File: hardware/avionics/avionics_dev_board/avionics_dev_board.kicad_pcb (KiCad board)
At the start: 4 copper layers, 113.6 x 79.4 mm, 78 parts, among them IC1 ADXL375BCCZ, IC2 W25Q256JVEIQ, J1 Main battery, J10 Parachute battery, J2 LAMBDA62, J3 Conn_01x08_Socket, J4 LAMBDA80, J5 Conn_01x08_Socket, J6 SWD interface, J7 868MHz antenna, J8 2.4GHz antenna, J9 Nichrome connector, Q3 FDS2734, SW2 SW_SPDT, SW3 SW_SPDT, SW4 SW_Push, SW5 SW_SPDT, U1 TPS563200, U2 MMC5983MA, U3 LSM6DSR, U4 BMP581, U6 MAX-M10S-00B, U7 STM32G474RET6, Y1 16MHz

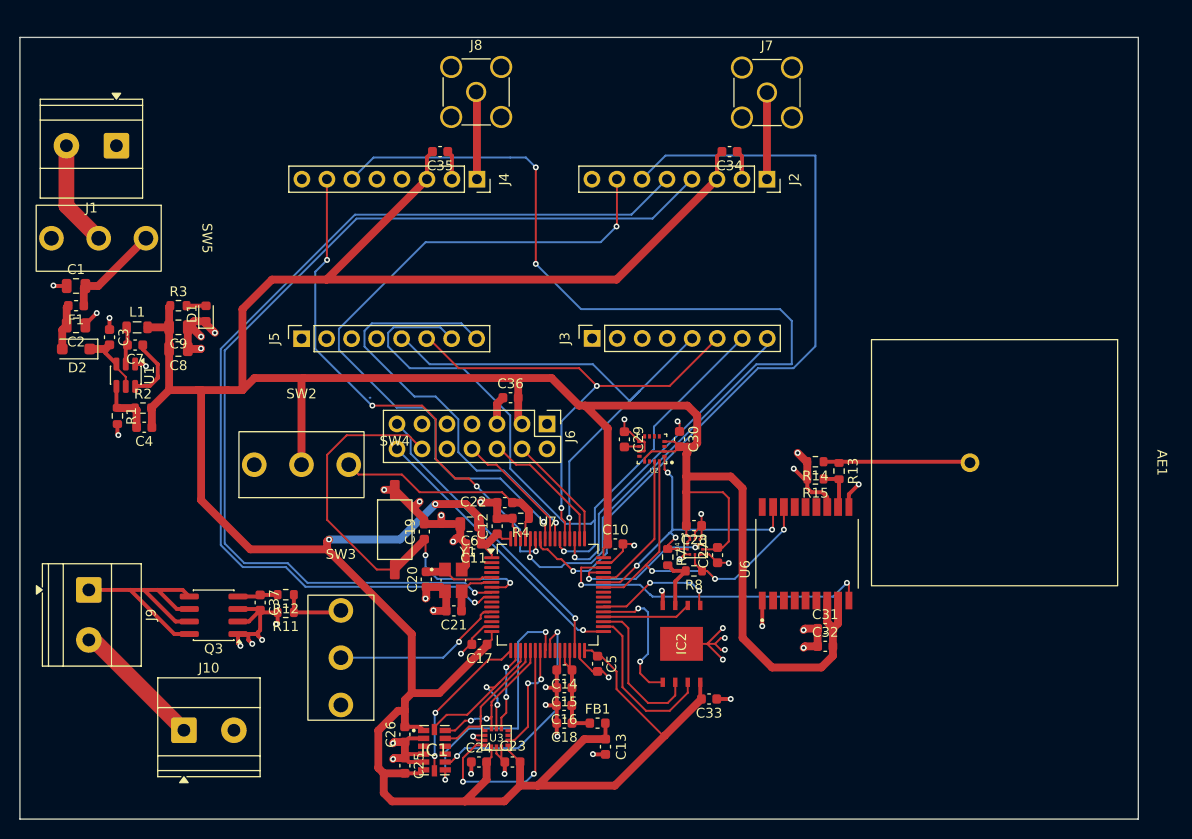
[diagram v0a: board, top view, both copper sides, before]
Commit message: Avionics dev PCB revision 2 - improved stackup and routing
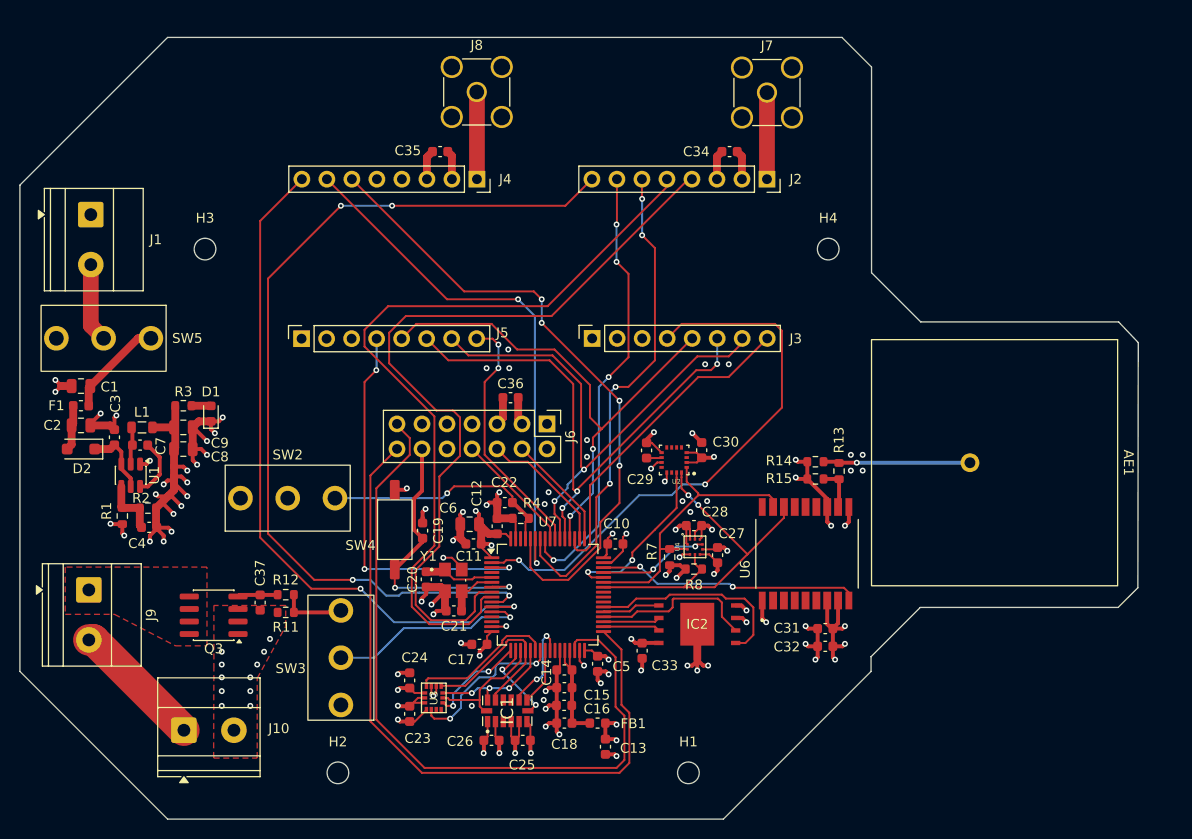
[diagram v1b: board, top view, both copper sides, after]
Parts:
- added H1: MountingHole, MountingHole:MountingHole_2.2mm_M2, F.Cu at (166.5, 102.5)
- added H2: MountingHole, MountingHole:MountingHole_2.2mm_M2, F.Cu at (130.9, 102.5)
- added H3: MountingHole, MountingHole:MountingHole_2.2mm_M2, F.Cu at (117.4, 49.3)
- added H4: MountingHole, MountingHole:MountingHole_2.2mm_M2, F.Cu at (180.7, 49.3)
- moved C25 12.2 mm to (149.7, 99.2), turned to 0 degrees
- moved C23 11.5 mm to (138.2, 96.5), turned to -90 degrees
- moved C24 10.9 mm to (138.2, 93.1), turned to -90 degrees
- moved C2 10.2 mm to (104.8, 67.2)
- moved C7 10.2 mm to (110.8, 69.2)
- moved F1 10.2 mm to (104.8, 65.2)
- moved R3 10.2 mm to (115.2, 65.2)
- moved U1 10.2 mm to (109.8, 72.3)
- moved C1 10.2 mm to (104.8, 63.2)
- moved D1 10.2 mm to (118.0, 66.0)
- moved C3 10.2 mm to (108.2, 68.4)
- moved C4 10.2 mm to (111.7, 77.6)
- moved C8 10.2 mm to (115.2, 69.6)
- moved C9 10.2 mm to (115.2, 67.4)
- moved D2 10.2 mm to (104.8, 69.6)
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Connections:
- net Net-(J10-Pin_1) renamed /PARA_PWR
- net Net-(J9-Pin_1) renamed /PARA_GND
- J3 pad 1: /L62_DIO3 -> unconnected-(J3-Pin_1-Pad1)
- J5 pad 1: /L80_DIO3 -> unconnected-(J5-Pin_1-Pad1)
- U7 pad 10: /L62_DIO3 -> /L62_DIO2
- U7 pad 11: /L80_DIO3 -> /L80_DIO2
- U7 pad 17: /CS_ADXL -> /CS_LSM6
- U7 pad 18: /CS_LSM6 -> /CS_ADXL
- U7 pad 4: /L62_DIO2 -> unconnected-(U7-PC15-Pad4)
- U7 pad 62: /L80_DIO2 -> unconnected-(U7-PB9-Pad62)
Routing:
- net +3V3: track 439.4 -> 110.8 mm, vias 2 -> 32
- net /L62_DIO2: track 0.00 -> 92.4 mm, vias 0 -> 4
- net /L80_DIO2: track 0.15 -> 70.5 mm, vias 0 -> 2
- net /L62_RST: track 0.00 -> 57.2 mm, vias 0 -> 2
- net /VCP_RX: track 30.7 -> 76.2 mm, vias 1 -> 0
- net /VCP_TX: track 28.7 -> 72.1 mm, vias 1 -> 0
- net /L80_RST: track 0.00 -> 40.4 mm, vias 0 -> 3
- net /L80_BUSY: track 102.1 -> 65.6 mm, vias 3 -> 4
- net /L62_BUSY: track 79.2 -> 50.5 mm, vias 1 -> 4
- net /PARA_GND: track 28.3 -> 0.00 mm
- net /L62_DIO1: track 71.6 -> 45.5 mm, vias 2 -> 4
- net /L62_RXSW: track 103.5 -> 81.1 mm, vias 1 -> 0
- net /L62_TXSW: track 102.6 -> 80.3 mm, vias 1 -> 0
- net /INT1_ADXL: track 26.1 -> 5.79 mm, vias 2 -> 0
- net /L80_CS: track 44.4 -> 25.7 mm, vias 1 -> 2
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- added copper zone on In2.Cu, net +3V3
- added copper zone on F.Cu, net /PARA_GND
- added copper zone on F.Cu, net GND
- removed copper zone on In2.Cu, net GND
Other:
- outline, holes or cut-outs redrawn

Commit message: Cleanup and refinements to avionics dev board PCB
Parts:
- moved C4 104.8 mm to (207.9, 36.2), turned to -90 degrees
- moved R1 104.8 mm to (206.8, 38.9), turned to 0 degrees
- moved R2 102.3 mm to (206.0, 36.3), turned to 90 degrees
- moved J1-MBAT 99.6 mm to (205.1, 53.9), turned to 90 degrees
- moved BUCK 98.9 mm to (202.7, 38.0), turned to 0 degrees
- moved D2 98.8 mm to (200.0, 43.1), turned to -90 degrees
- moved C2 95.9 mm to (197.6, 43.1), turned to -90 degrees
- moved C3 95.0 mm to (198.8, 39.7), turned to 0 degrees
- moved C7 94.4 mm to (199.6, 37.1), turned to -90 degrees
- moved F1 93.5 mm to (195.6, 43.1), turned to -90 degrees
- moved C8 92.5 mm to (200.0, 32.7), turned to -90 degrees
- moved L1 92.0 mm to (197.8, 36.9), turned to 90 degrees
- moved C1 91.1 mm to (193.6, 43.1), turned to 90 degrees
- moved C9 89.6 mm to (197.8, 32.7), turned to -90 degrees
- moved R3 86.7 mm to (195.6, 32.7), turned to 90 degrees
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- renumbered IC1 to ADXL, J8 to ANT_24, J7 to ANT_868, U4 to BMP1, SW2 to BOOT_SW, U1 to BUCK, J1 to J1-MBAT, J10 to J10-PBAT, J9 to J9-NICH, J2 to L62-1, J3 to L62-2, J4 to L80-1, J5 to L80-2, U3 to LSM6, U6 to M10S, U7 to MCU, U2 to MMC, SW3 to PARA_ARM, D1 to PWR_LED, SW5 to PWR_SW, SW4 to RST, J6 to SWD_INT, IC2 to W25Q
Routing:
- net Net-(PARA_ARM1-C): track 6.66 -> 55.0 mm, vias 0 -> 1
- net Net-(J1-MBAT1-Pin_2): track 8.02 -> 27.8 mm
- net /PARA_PWR: track 13.5 -> 6.96 mm
- net /SPI1_SCK: track 12.8 -> 13.7 mm, vias 0 -> 1
- net /I2C2_SCL: track 30.4 -> 30.5 mm, vias 0 -> 1
- net /LSM6_INT1: vias 0 -> 1
- net /L62_CS: vias 0 -> 1
- net GND: vias 86 -> 189
- net /SPI2_SCK: vias 0 -> 1
- net /SPI2_MOSI: vias 0 -> 1
- net /SPI2_MISO: vias 0 -> 1
- net /SPI1_MISO: vias 0 -> 1
- net /RST_W25Q: vias 0 -> 1
- net /L62_TXSW: vias 0 -> 1
- net /L62_RXSW: vias 0 -> 1
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- added copper zone on B.Cu, net GND
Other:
- board size 113.6 x 79.4 mm -> 91.5 x 78.9 mm

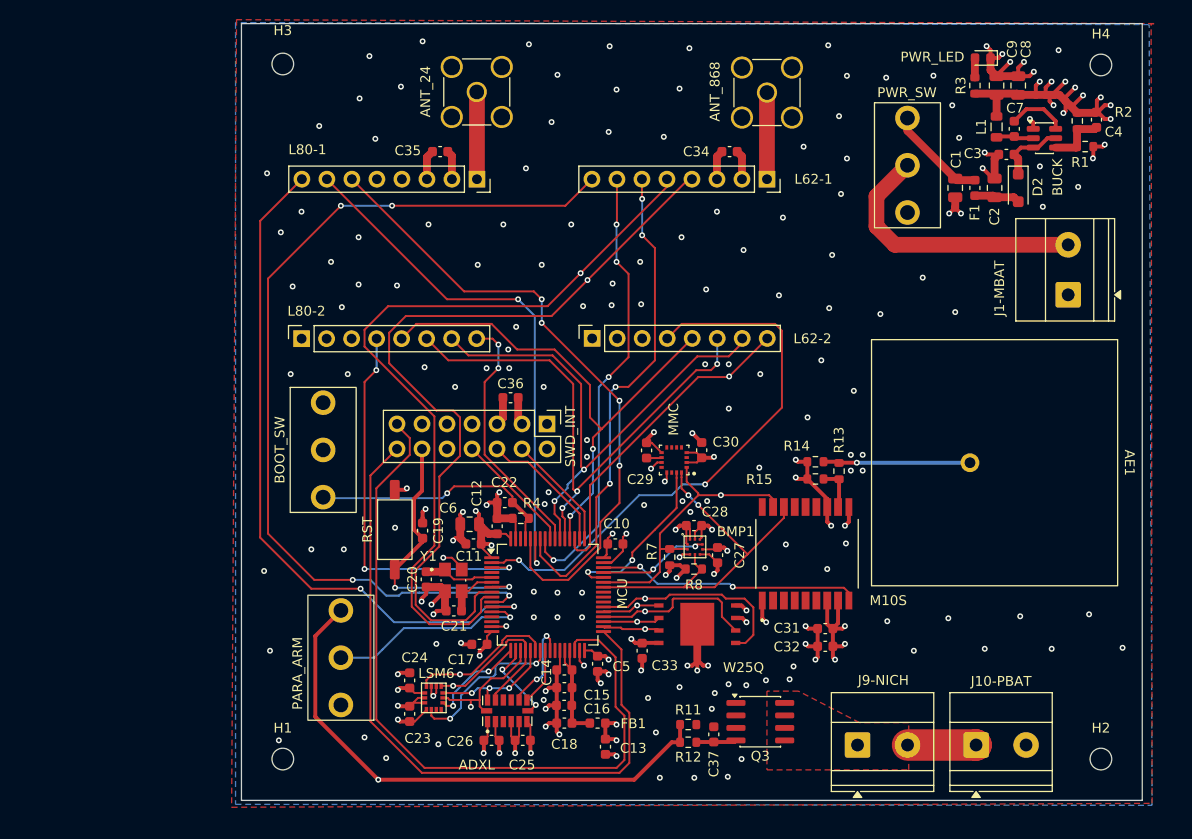
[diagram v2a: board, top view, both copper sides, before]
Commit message: Improved shielding of GPS RF trace and added 0 ohm resistors to switch SWD RX and TX if necessary
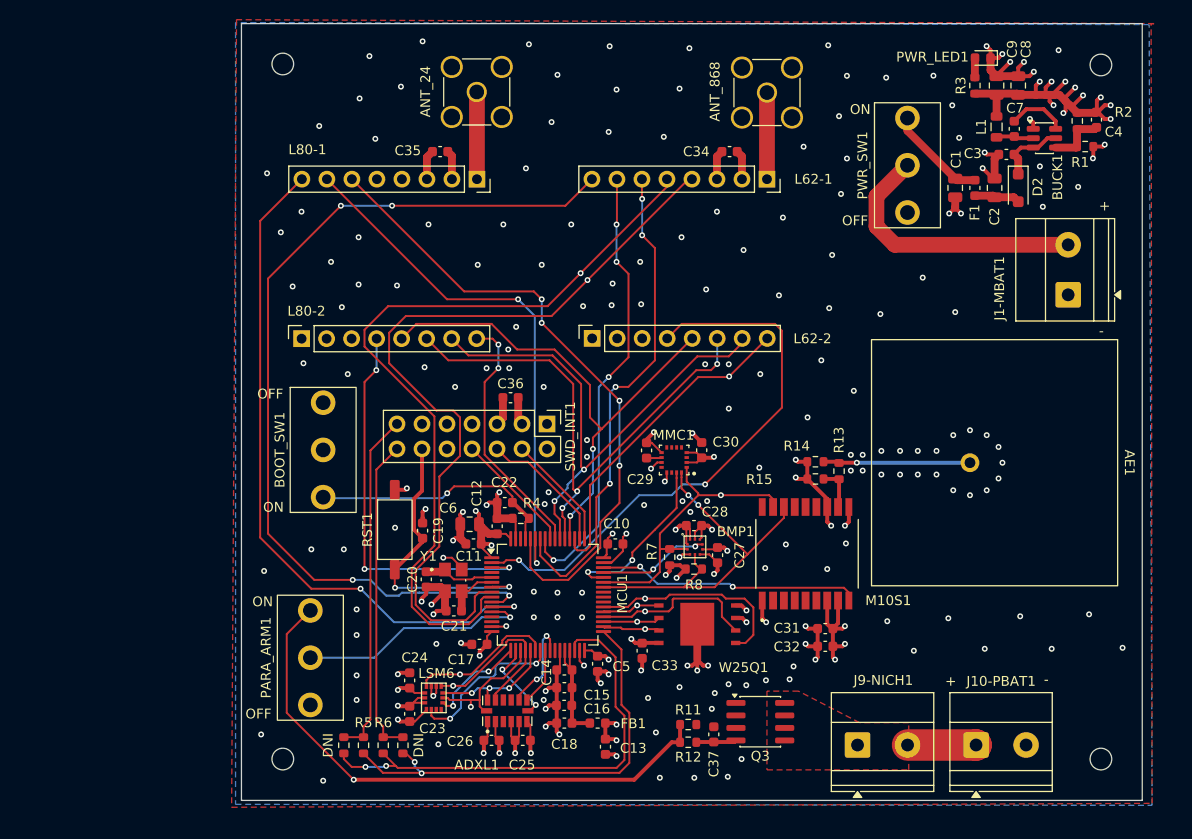
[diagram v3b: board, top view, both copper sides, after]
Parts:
- added DNI: 0R, Resistor_SMD:R_0603_1608Metric, F.Cu at (131.5, 99.7)
- added DNI: 0R, Resistor_SMD:R_0603_1608Metric, F.Cu at (137.5, 99.7)
- added R5: 0R, Resistor_SMD:R_0603_1608Metric, F.Cu at (133.5, 99.7)
- added R6: 0R, Resistor_SMD:R_0603_1608Metric, F.Cu at (135.5, 99.7)
- C20, C21: value 10pF -> 12pF
- moved PARA_ARM1 3.10 mm to (128.1, 90.8)
- renumbered ADXL to ADXL1, BOOT_SW to BOOT_SW1, BUCK to BUCK1, J1-MBAT to J1-MBAT1, J10-PBAT to J10-PBAT1, J9-NICH to J9-NICH1, M10S to M10S1, MCU to MCU1, MMC to MMC1, PARA_ARM to PARA_ARM1, PWR_LED to PWR_LED1, PWR_SW to PWR_SW1, RST to RST1, SWD_INT to SWD_INT1, W25Q to W25Q1
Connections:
- MCU1 pad 30: /VCP_RX -> /VCP_TX
- MCU1 pad 33: /VCP_TX -> /VCP_RX
- SWD_INT1 pad 13: /VCP_RX -> Net-(SWD_INT1-Pin_13)
- SWD_INT1 pad 14: /VCP_TX -> Net-(SWD_INT1-Pin_14)
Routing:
- net Net-(SWD_INT1-Pin_13): track 0.00 -> 35.4 mm
- net Net-(SWD_INT1-Pin_14): track 0.00 -> 32.4 mm
- net /VCP_RX: track 76.2 -> 45.7 mm, vias 0 -> 2
- net /VCP_TX: track 72.1 -> 48.3 mm, vias 0 -> 2
- net /PARA_DEPLOY: track 21.0 -> 24.1 mm
- net Net-(PARA_ARM1-C): track 55.0 -> 57.5 mm
- net GND: vias 189 -> 208
- added copper zone on In2.Cu, net GND
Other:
- board text added: "+"
- board text added: "-"
- board text added: "OFF"
- board text added: "ON"

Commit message: Added pull up/down resistors to some pins according to datasheet recommendations
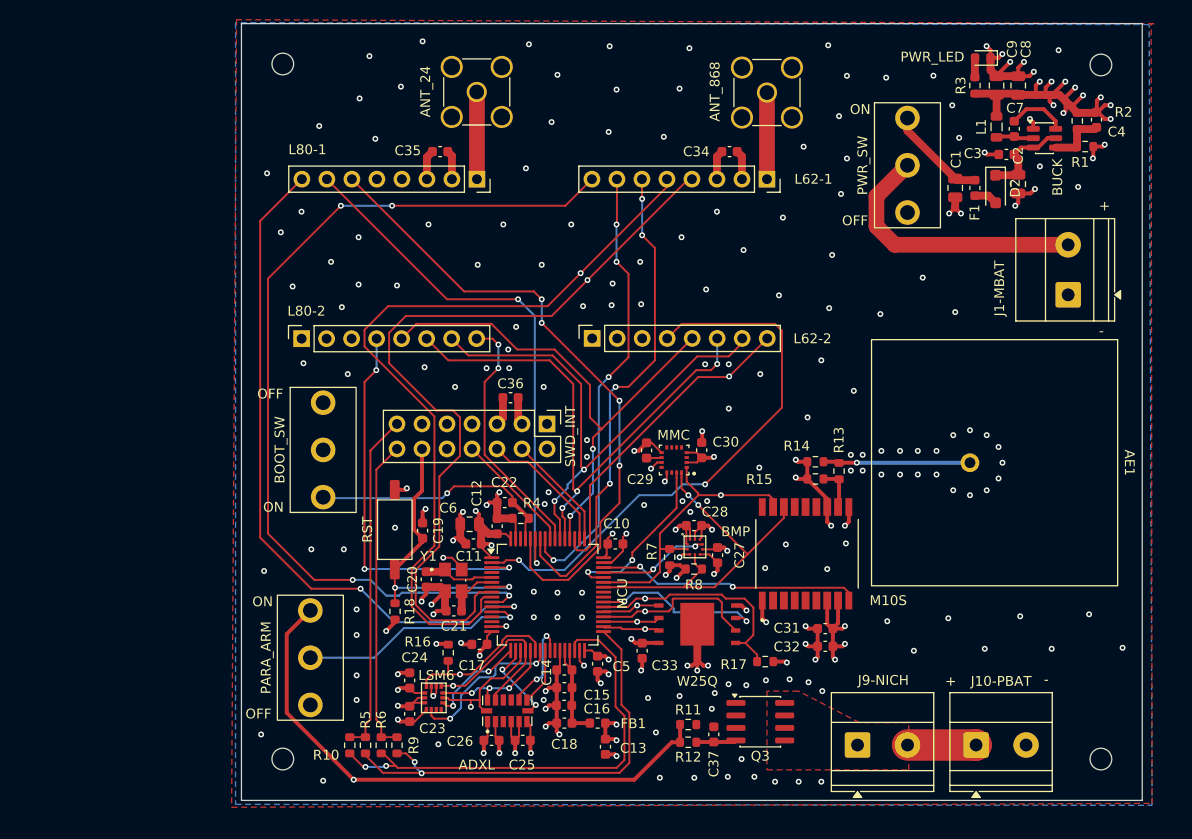
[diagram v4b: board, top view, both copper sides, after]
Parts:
- added R16: 10kR, Resistor_SMD:R_0603_1608Metric, F.Cu at (142.1, 90.3)
- added R17: 10kR, Resistor_SMD:R_0603_1608Metric, F.Cu at (174.3, 91.2)
- added R18: 10kR, Resistor_SMD:R_0603_1608Metric, F.Cu at (136.7, 86.1)
- moved C2 2.43 mm to (200.0, 42.7), turned to 90 degrees
- moved D2 2.30 mm to (197.7, 43.2)
- moved R10 0.60 mm to (132.1, 99.7)
- moved R9 0.60 mm to (136.9, 99.7)
- moved R5 0.20 mm to (133.7, 99.7)
- moved R6 0.20 mm to (135.3, 99.7)
- renumbered ADXL1 to ADXL, BMP1 to BMP, BOOT_SW1 to BOOT_SW, BUCK1 to BUCK, J1-MBAT1 to J1-MBAT, J10-PBAT1 to J10-PBAT, J9-NICH1 to J9-NICH, M10S1 to M10S, MCU1 to MCU, MMC1 to MMC, PARA_ARM1 to PARA_ARM, PWR_LED1 to PWR_LED, PWR_SW1 to PWR_SW, DNI to R10, DNI to R9, RST1 to RST, SWD_INT1 to SWD_INT, W25Q1 to W25Q
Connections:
- net /RST_W25Q renamed /HOLD_W25Q
- C2 pad 2: Net-(D2-A) -> Net-(BUCK1-EN)
- MCU pad 39: unconnected-(MCU1-PC7-Pad39) -> /WP_W25Q
- W25Q pad 3: +3V3 -> /WP_W25Q
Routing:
- net /WP_W25Q: track 0.00 -> 17.6 mm, vias 0 -> 2
- net Net-(BUCK1-EN): track 7.08 -> 9.63 mm
- net /CS_W25Q: track 21.2 -> 23.6 mm
- net Net-(D2-A): track 4.65 -> 2.40 mm
- net +3V3: track 110.8 -> 112.4 mm, vias 32 -> 33
- net /NRST: track 29.6 -> 31.2 mm
- net /LSM6_INT1: track 14.8 -> 15.8 mm
- net /VCP_TX: track 48.3 -> 47.3 mm
- net /VCP_RX: track 45.7 -> 46.3 mm
- net GND: track 148.3 -> 148.6 mm, vias 208 -> 213

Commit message: Log file update
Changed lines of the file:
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@@
 		(pad_to_mask_clearance 0)
 		(allow_soldermask_bridges_in_footprints no)
-		(tenting front back)
+		(tenting none)
 		(pcbplotparams
 			(layerselection 0x00000000_00000000_55555555_5755f5ff)
 			(plot_on_all_layers_selection 0x00000000_00000000_00000000_00000000)
 			(disableapertmacros no)
-			(usegerberextensions no)
+			(usegerberextensions yes)
 			(usegerberattributes yes)
 			(usegerberadvancedattributes yes)
@@
 		(tags "D_SOD-123F")
 		(property "Reference" "D2"
-			(at -0.1 -1.9875 90)
+			(at 3.1 0 90)
 			(layer "F.SilkS")
 			(effects

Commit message: Avionics dev board V2
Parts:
- added C38: 100nF, Capacitor_SMD:C_0603_1608Metric, F.Cu at (166.4, 97.8)
- added J1-MCU: Conn_01x02, Connector_PinHeader_2.54mm:PinHeader_1x02_P2.54mm_Vertical, F.Cu at (152.8, 69.2)
- added J2-ACC: Conn_01x02, Connector_PinHeader_2.54mm:PinHeader_1x02_P2.54mm_Vertical, F.Cu at (140.5, 100.0)
- added J4-PMAG: Conn_01x02, Connector_PinHeader_2.54mm:PinHeader_1x02_P2.54mm_Vertical, F.Cu at (168.7, 65.4)
- added J6-M10S: Conn_01x02, Connector_PinHeader_2.54mm:PinHeader_1x02_P2.54mm_Vertical, F.Cu at (185.9, 90.2)
- added J7-W25Q: Conn_01x02, Connector_PinHeader_2.54mm:PinHeader_1x02_P2.54mm_Vertical, F.Cu at (175.9, 93.7)
- added J8-L62: Conn_01x02, Connector_PinHeader_2.54mm:PinHeader_1x02_P2.54mm_Vertical, F.Cu at (159.9, 37.1)
- added J9-L80: Conn_01x02, Connector_PinHeader_2.54mm:PinHeader_1x02_P2.54mm_Vertical, F.Cu at (131.0, 37.3)
- added R19: 10kR, Resistor_SMD:R_0603_1608Metric, F.Cu at (162.3, 97.0)
- added R20: 220R, Resistor_SMD:R_0603_1608Metric, F.Cu at (171.0, 95.2)
- added TP-3V3: TestPoint, TestPoint:TestPoint_Pad_D1.0mm, F.Cu at (137.6, 64.2)
- added TP-GND: TestPoint, TestPoint:TestPoint_Pad_D1.0mm, F.Cu at (140.9, 64.2)
- added UBT: SW_Push, avionicsw:hanxia HX 3x4x2-2P-1.6N TACTILE SWITCH, F.Cu at (166.4, 95.3)
- added ULED: PWR LED, LED_SMD:LED_0603_1608Metric, F.Cu at (172.7, 95.3)
- BUCK: value TPS563200 -> TPS563208
- R3: value 1kR -> 220R
- RST1: renamed from RST; footprint avionicsw:G-Switch GT-TC060A-H025-L1S -> avionicsw:hanxia HX 3x4x2-2P-1.6N TACTILE SWITCH
- SWD_INT: footprint Connector_PinHeader_2.54mm:PinHeader_2x07_P2.54mm_Vertical -> Connector_PinSocket_1.27mm:PinSocket_2x07_P1.27mm_Vertical
- moved C36 8.76 mm to (143.3, 71.5)
- moved SWD_INT 7.43 mm to (145.0, 69.0)
- moved C37 3.59 mm to (169.2, 102.2)
- moved R11 3.59 mm to (166.6, 101.2)
- moved R12 3.59 mm to (166.6, 103.0)
- moved Q3 3.59 mm to (173.9, 100.9)
- moved C34 0.60 mm to (170.7, 38.8)
- moved L62-1 0.60 mm to (174.4, 41.6)
- moved C35 0.60 mm to (141.3, 38.8)
- moved L80-1 0.60 mm to (145.0, 41.6)
- moved C27 0.51 mm to (169.5, 80.9)
- moved RST1 0.40 mm to (136.7, 78.2), turned to 90 degrees
- moved R17 0.30 mm to (174.3, 90.9)
- moved C4 0.14 mm to (207.9, 36.3)
- renumbered J1-MBAT to T1-MBAT, J10-PBAT to T2-PBAT, J9-NICH to T3-NICH
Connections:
- ADXL pad 1: +3V3 -> /VCC-ACC
- ADXL pad 6: +3V3 -> /VCC-ACC
- BMP pad 1: +3V3 -> /VCC-PMAG
- BMP pad 10: +3V3 -> /VCC-PMAG
- BMP pad 6: +3V3 -> /VCC-PMAG
- C10 pad 1: +3V3 -> /VCC-MCU
- C11 pad 1: +3V3 -> /VCC-MCU
- C12 pad 1: +3V3 -> /VCC-MCU
- C13 pad 1: +3V3 -> /VCC-MCU
- C17 pad 1: +3V3 -> /VCC-MCU
- C23 pad 2: +3V3 -> /VCC-ACC
- C24 pad 2: +3V3 -> /VCC-ACC
- C25 pad 2: +3V3 -> /VCC-ACC
- C26 pad 2: +3V3 -> /VCC-ACC
- C27 pad 2: +3V3 -> /VCC-PMAG
- C28 pad 2: +3V3 -> /VCC-PMAG
- C30 pad 2: +3V3 -> /VCC-PMAG
- C31 pad 2: +3V3 -> /VCC-M10S
- C32 pad 2: +3V3 -> /VCC-M10S
- C33 pad 2: +3V3 -> /VCC-W25Q
- C34 pad 2: +3V3 -> /L62_VCC
- C35 pad 2: +3V3 -> /L80_VCC
- C5 pad 1: +3V3 -> /VCC-MCU
- C6 pad 1: +3V3 -> /VCC-MCU
- FB1 pad 2: +3V3 -> /VCC-MCU
- L62-1 pad 3: +3V3 -> /L62_VCC
- L80-1 pad 3: +3V3 -> /L80_VCC
- LSM6 pad P$5: +3V3 -> /VCC-ACC
- LSM6 pad P$8: +3V3 -> /VCC-ACC
- M10S pad 7: +3V3 -> /VCC-M10S
- M10S pad 8: +3V3 -> /VCC-M10S
- MCU pad 1: +3V3 -> /VCC-MCU
- MCU pad 16: +3V3 -> /VCC-MCU
- MCU pad 32: +3V3 -> /VCC-MCU
- MCU pad 40: unconnected-(MCU1-PC8-Pad40) -> Net-(MCU1-PC8)
- MCU pad 41: unconnected-(MCU1-PC9-Pad41) -> Net-(MCU1-PC9)
- MCU pad 48: +3V3 -> /VCC-MCU
- MCU pad 64: +3V3 -> /VCC-MCU
- MMC pad 13: +3V3 -> /VCC-PMAG
- MMC pad 2: +3V3 -> /VCC-PMAG
- MMC pad 4: +3V3 -> /VCC-PMAG
- R17 pad 2: +3V3 -> /VCC-W25Q
- R7 pad 2: +3V3 -> /VCC-PMAG
- R8 pad 2: +3V3 -> /VCC-PMAG
- W25Q pad 8: +3V3 -> /VCC-W25Q
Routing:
- net +3V3: track 112.4 -> 40.9 mm, vias 33 -> 15
- net Net-(MCU1-PC9): track 0.00 -> 23.5 mm, vias 0 -> 2
- net Net-(MCU1-PC8): track 0.00 -> 23.4 mm, vias 0 -> 2
- net /VCC-MCU: track 0.00 -> 22.8 mm, vias 0 -> 7
- net /VCC-W25Q: track 0.00 -> 18.8 mm
- net /VCC-M10S: track 0.00 -> 18.4 mm
- net /VCC-PMAG: track 0.00 -> 17.9 mm, vias 0 -> 6
- net /VCC-ACC: track 0.00 -> 13.2 mm, vias 0 -> 4
- net /SWO: track 12.4 -> 24.6 mm, vias 0 -> 1
- net /L62_VCC: track 0.00 -> 11.3 mm
- net /L80_VCC: track 0.00 -> 10.6 mm
- net /SWCLK: track 13.7 -> 23.3 mm, vias 0 -> 1
- net /SWDIO: track 11.8 -> 19.6 mm, vias 0 -> 1
- net /NRST: track 31.2 -> 37.8 mm, vias 2 -> 3
- net /L62_RXSW: track 81.1 -> 86.3 mm, vias 1 -> 2
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- added copper zone on In2.Cu, net /VCC-ACC
- added copper zone on In2.Cu, net /VCC-MCU
- added copper zone on In2.Cu, net /VCC-PMAG
